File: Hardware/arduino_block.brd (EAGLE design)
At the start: 30.5 x 62.2 mm, 40 parts, among them U1 MIC5205-3.3V (150mA), U2 EDISON_CONNECTOR_FULLMOUNTING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, U3 EDISON_CONNECTOR_FULLHEADER, U4 ATMEGA328, Y1 8MHZ

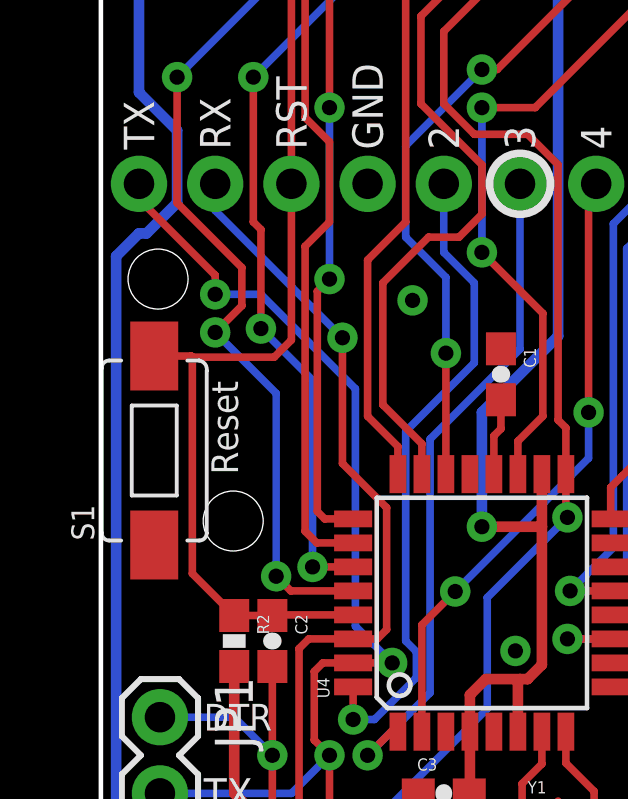
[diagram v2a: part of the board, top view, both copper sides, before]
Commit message: Replaced reset button with new RA SMD push button
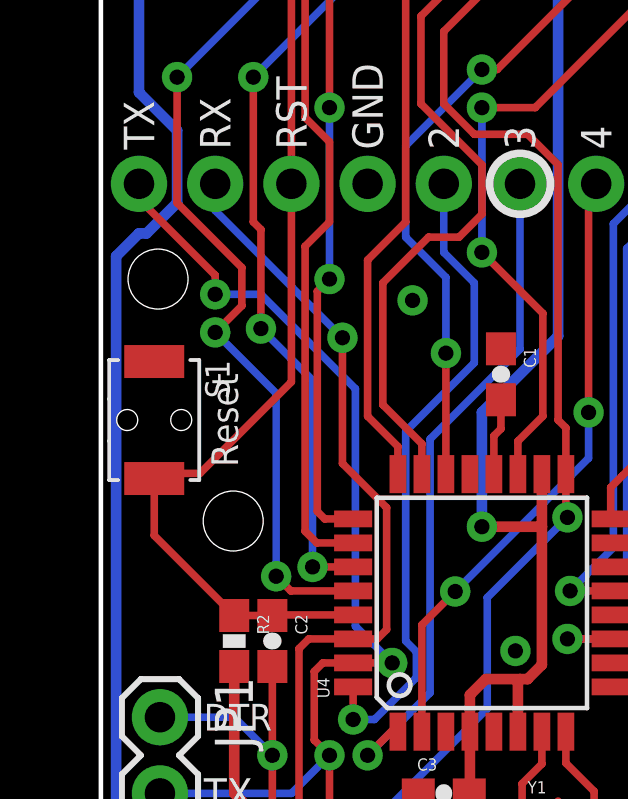
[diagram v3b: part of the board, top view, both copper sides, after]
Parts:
- S1: device SparkFun-Electromechanical:TACTILE-SWITCH-1101NE -> SparkFun-Electromechanical:TACTILE_SWITCH-SMD-RIGHT-ANGLE
- moved S1 1.02 mm to (1.78, 37.8), turned to 270 degrees
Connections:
- net GND: now also S1.1; no longer S1.P$1
- net RESET: now also S1.2; no longer S1.P$2
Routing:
- net RESET: track 38.5 -> 37.5 mm
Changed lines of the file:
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@@
 <?xml version="1.0" encoding="utf-8"?>
 <!DOCTYPE eagle SYSTEM "eagle.dtd">
-<eagle version="7.1.0">
+<eagle version="6.5.0">
 <drawing>
 <settings>
@@
 <setting verticaltext="up"/>
 </settings>
-<grid distance="0.05" unitdist="inch" unit="inch" style="lines" multiple="1" display="yes" altdistance="0.001" altunitdist="inch" altunit="inch"/>
+<grid distance="0.01" unitdist="inch" unit="inch" style="lines" multiple="1" display="yes" altdistance="0.001" altunitdist="inch" altunit="inch"/>
 <layers>
 <layer number="1" name="Top" color="4" fill="1" visible="yes" active="yes"/>
@@
 <text x="3.429" y="20.32" size="0.889" layer="21" font="vector" ratio="15" align="center-left">VCC</text>
 <text x="3.429" y="17.78" size="0.889" layer="21" font="vector" ratio="15" align="center-left">GND</text>
-<text x="3.683" y="37.592" size="0.889" layer="21" font="vector" ratio="15" rot="R90" align="top-center">Reset</text>
+<text x="3.683" y="37.846" size="0.889" layer="21" font="vector" ratio="15" rot="R90" align="top-center">Reset</text>
 <text x="3.429" y="15.875" size="0.889" layer="21" font="vector" ratio="15" align="center-left">GND</text>
 <text x="3.429" y="14.6685" size="0.889" layer="21" font="vector" ratio="15" align="center-left">BLK</text>
@@
 <pass name="Default">
 <param name="RoutingGrid" value="50mil"/>
-<param name="AutoGrid" value="1"/>
-<param name="Efforts" value="0"/>
-<param name="TopRouterVariant" value="1"/>
 <param name="tpViaShape" value="round"/>
 <param name="PrefDir.1" value="|"/>
@@
 <element name="JP1" library="SparkFun" package="1X06" value="FTDI Basic" x="1.9685" y="27.94" rot="R270"/>
 <element name="C2" library="SparkFun" package="0603-CAP" value="0.1uF" x="5.715" y="30.48" rot="R270"/>
-<element name="S1" library="SparkFun-Electromechanical" package="TACTILE-SWITCH-1101NE" value="RESET" x="1.778" y="36.83" rot="R90"/>
 <element name="Y1" library="SparkFun-FreqCtrl" package="RESONATOR-SMD" value="8MHZ" x="15.24" y="24.13">
 <attribute name="PROD_ID" value="XTAL-08895" x="15.24" y="24.13" size="1.778" layer="27" font="vector" ratio="15" display="off"/>
@@
 <element name="JP5" library="SparkFun-Connectors" package="1X02_NO_SILK" value="M021X02_NO_SILK" x="22.987" y="56.769" rot="R180"/>
 <element name="SJ5" library="SparkFun-Passives" package="PAD-JUMPER-2-NO_YES_SILK" value="DCIN" x="17.78" y="21.59" rot="MR90"/>
+<element name="S1" library="SparkFun-Electromechanical" package="TACTILE_SWITCH-SMD-RIGHT-ANGLE" value="RESET" x="1.778" y="37.846" rot="R270">
+<attribute name="PROD_ID" value="COMP-12265" x="1.778" y="37.846" size="1.778" layer="27" rot="R270" display="off"/>
+</element>
 </elements>
 <signals>
@@
 <contactref element="JP1" pad="6"/>
 <contactref element="R11" pad="1"/>
-<contactref element="S1" pad="P$1"/>
 <contactref element="Y1" pad="2"/>
 <contactref element="C5" pad="1"/>
@@
 <contactref element="JP3" pad="4"/>
 <via x="10.3886" y="41.8338" extent="1-16" drill="0.508"/>
+<contactref element="S1" pad="1"/>
 </signal>
 <signal name="VSYS">
@@
 <contactref element="R2" pad="1"/>
 <contactref element="C2" pad="1"/>
-<contactref element="S1" pad="P$2"/>
 <wire x1="8.4074" y1="31.35" x2="5.735" y2="31.35" width="0.254" layer="1"/>
 <wire x1="5.735" y1="31.35" x2="5.715" y2="31.33" width="0.254" layer="1"/>
 <wire x1="5.715" y1="31.33" x2="4.445" y2="31.33" width="0.254" layer="1"/>
 <wire x1="4.445" y1="31.2674" x2="4.445" y2="31.33" width="0.254" layer="1"/>
-<wire x1="1.778" y1="39.98" x2="3.0095" y2="39.98" width="0.254" layer="1"/>
-<wire x1="3.0095" y1="39.98" x2="3.048" y2="39.9415" width="0.254" layer="1"/>
-<wire x1="3.048" y1="32.727" x2="4.445" y2="31.33" width="0.254" layer="1"/>
-<wire x1="3.048" y1="32.727" x2="3.048" y2="39.9415" width="0.254" layer="1"/>
+<wire x1="1.778" y1="33.997" x2="4.445" y2="31.33" width="0.254" layer="1"/>
 <contactref element="JP2" pad="3"/>
 <contactref element="JP3" pad="3"/>
 <wire x1="6.35" y1="45.72" x2="6.35" y2="60.96" width="0.254" layer="1"/>
-<wire x1="6.35" y1="45.72" x2="6.35" y2="40.513" width="0.254" layer="1"/>
-<wire x1="6.35" y1="40.513" x2="5.7785" y2="39.9415" width="0.254" layer="1"/>
-<wire x1="3.048" y1="39.9415" x2="5.7785" y2="39.9415" width="0.254" layer="1"/>
+<wire x1="6.35" y1="45.72" x2="6.35" y2="39.116" width="0.254" layer="1"/>
+<contactref element="S1" pad="2"/>
+<wire x1="1.778" y1="33.997" x2="1.778" y2="35.896" width="0.254" layer="1"/>
+<wire x1="1.778" y1="35.896" x2="1.95" y2="36.068" width="0.254" layer="1"/>
+<wire x1="1.95" y1="36.068" x2="3.302" y2="36.068" width="0.254" layer="1"/>
+<wire x1="3.302" y1="36.068" x2="6.35" y2="39.116" width="0.254" layer="1"/>
 </signal>
 <signal name="SCK">
